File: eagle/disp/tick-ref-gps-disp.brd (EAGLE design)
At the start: 83.8 x 106.3 mm, 37 parts, among them CN1 To Main Board, Q1 MMBT3904, U1 AS1115, U2 AS1115

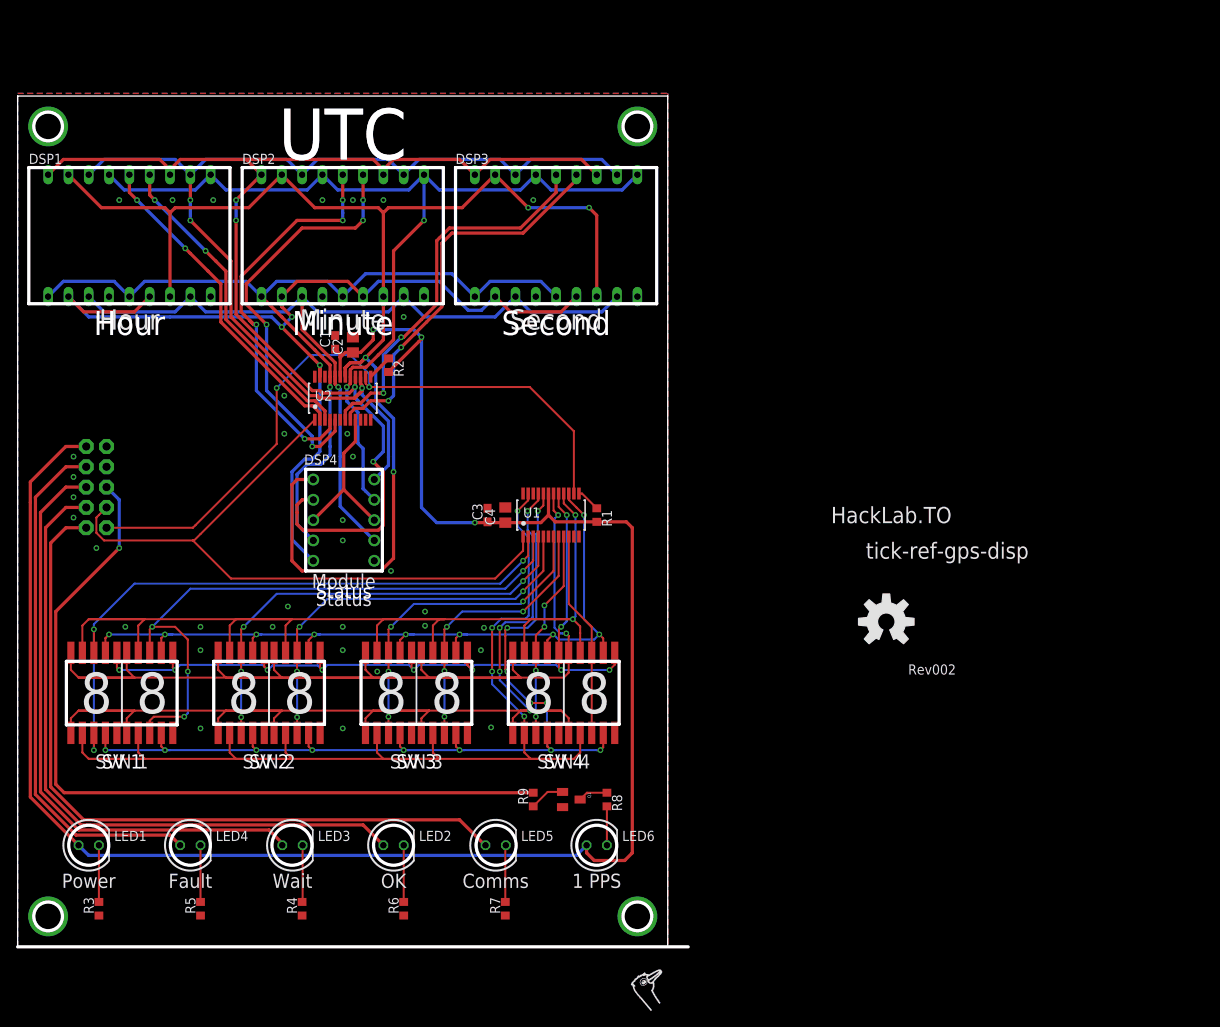
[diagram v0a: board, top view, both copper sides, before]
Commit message: Finally got around to measuring the actual enclosure, made the board the final width, switched to larger time displays, and rerouted for this. Still have to rearrange silk and make board slightly less tall to fit.
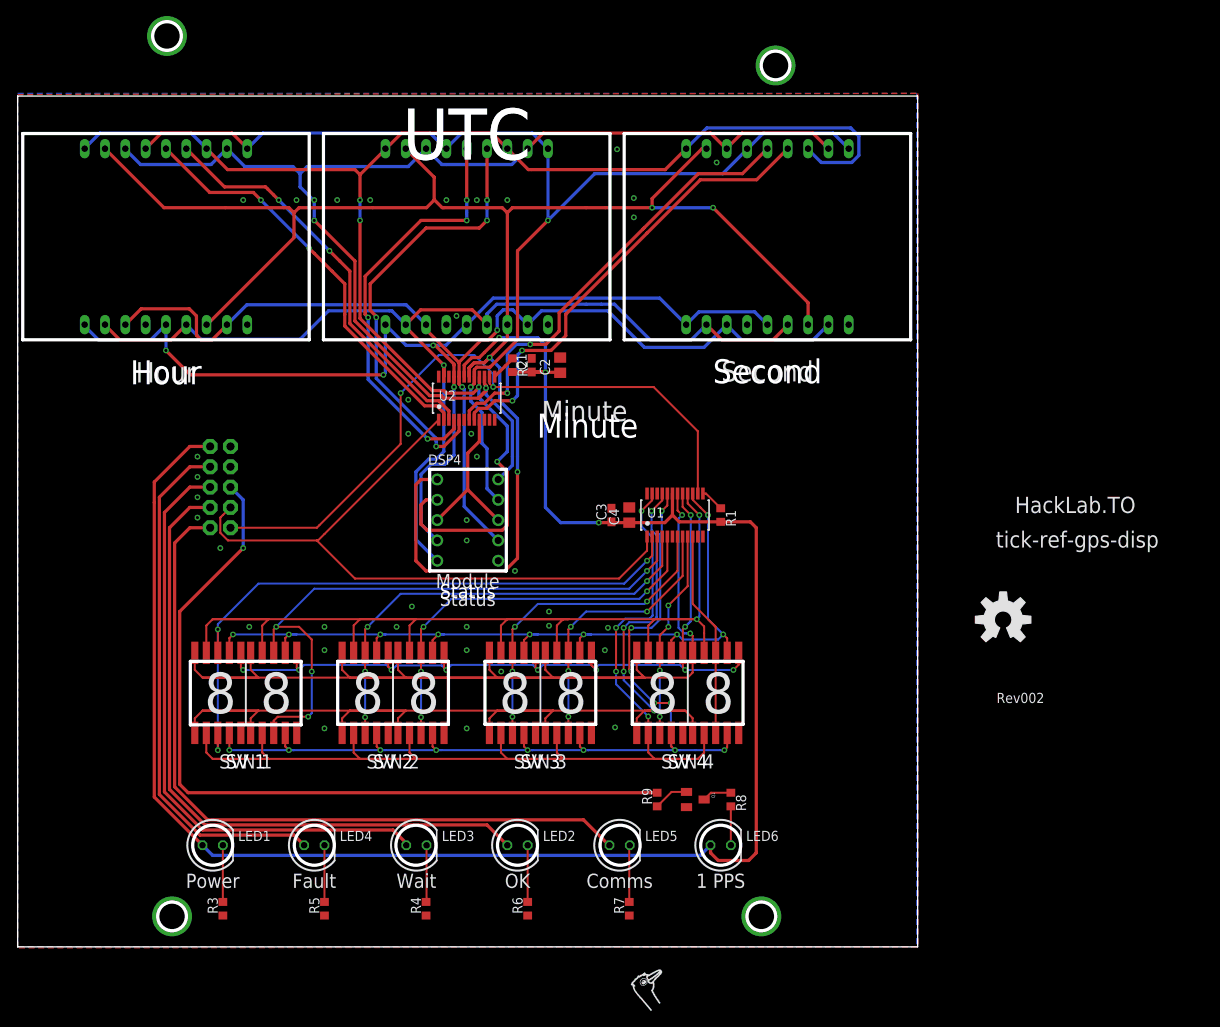
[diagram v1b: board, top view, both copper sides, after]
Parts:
- DSP1, DSP2, DSP3: device display-hp:HDSP-R -> led-sen:LUMEX-LDD-C81XRI
- moved DSP3 26.4 mm to (93.7, 88.8)
- moved C2 26.0 mm to (67.8, 72.7)
- moved C1 24.7 mm to (64.3, 72.7)
- moved DSP2 15.5 mm to (56.1, 88.8)
- moved LED4 15.5 mm to (37.1, 12.7)
- moved CN1 15.5 mm to (25.3, 57.5)
- moved DSP5 15.5 mm to (25.1, 31.8)
- moved C3 15.5 mm to (74.2, 54.0)
- moved DSP10 15.5 mm to (69.0, 31.8)
- moved DSP11 15.5 mm to (80.4, 31.8)
- moved DSP12 15.5 mm to (87.4, 31.8)
- moved DSP4 15.5 mm to (56.3, 53.3)
- moved DSP6 15.5 mm to (32.1, 31.8)
- moved DSP7 15.5 mm to (43.6, 31.8)
- moved DSP8 15.5 mm to (50.5, 31.8)
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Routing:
- net DSPA_SEG_G: track 176.9 -> 217.7 mm
- net DSPA_SEG_F: track 153.6 -> 191.6 mm
- net DSPA_SEG_B: track 121.1 -> 148.6 mm
- net DSPA_SEG_A: track 131.5 -> 155.9 mm
- net DSPA_SEG_E: track 109.8 -> 133.1 mm, vias 1 -> 4
- net DSPA_SEG_C: track 108.7 -> 131.3 mm, vias 1 -> 2
- net CATH_HOUR_MS: track 41.1 -> 52.4 mm
- net CATH_HOUR_LS: track 40.3 -> 51.3 mm
- net DSPA_SEG_D: track 125.0 -> 135.1 mm, vias 3 -> 1
- net CATH_SEC_LS: track 49.9 -> 58.2 mm
- net CATH_SEC_MS: track 48.7 -> 56.2 mm
- net CATH_MIN_LS: track 52.4 -> 55.7 mm
- net +5V: track 244.2 -> 241.8 mm
- net CATH_MIN_MS: track 50.9 -> 53.1 mm
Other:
- board size 83.8 x 106.3 mm -> 112.5 x 115.7 mm
